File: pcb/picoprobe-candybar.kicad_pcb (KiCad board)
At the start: 2 copper layers, 27.9 x 97 mm, 39 parts, among them J0 SWD-UART_PicoprobeCandybar, J1 PinHeader_2x04, J2 PinSocket_1x03, J3 PinSocket_1x03, J4 PinSocket_1x03, J5 PinSocket_1x03, J6 PinSocket_1x03, J7 PinSocket_1x03, Q1 T2N7002AK, Q2 DMP31D1U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

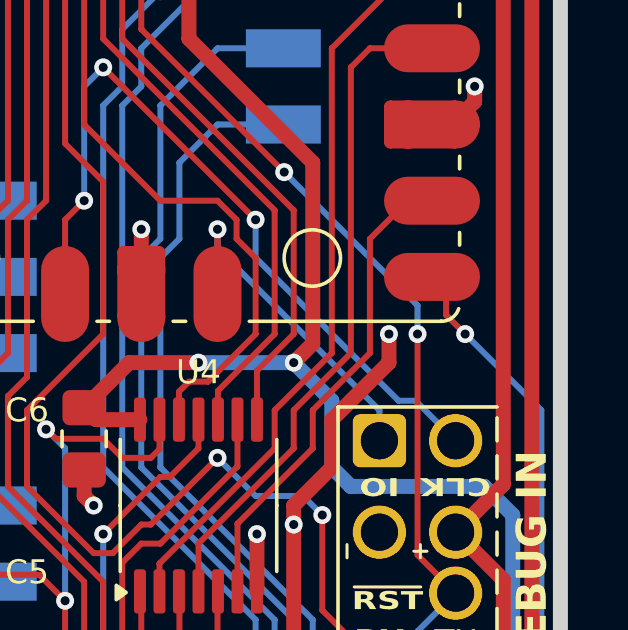
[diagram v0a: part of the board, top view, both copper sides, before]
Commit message: Change Q2 out for an available alternative
Original DMP31D1U was on backorder on Digi-Key.
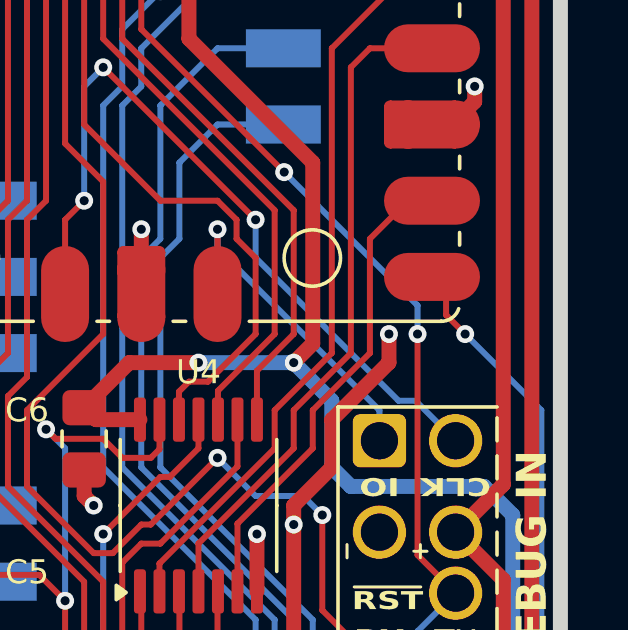
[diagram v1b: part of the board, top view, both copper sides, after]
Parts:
- Q2: value DMP31D1U -> GSFC02501
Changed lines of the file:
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@@
 		(fp_arc
 			(start 10.579676 25.189937)
-			(mid 10.357946 25.493957)
+			(mid 10.357958 25.493991)
 			(end 10 25.61)
 			(stroke
@@
 			)
 		)
-		(property "Value" "DMP31D1U"
+		(property "Value" "GSFC02501"
 			(at 0 2.4 90)
 			(layer "F.Fab")
@@
 			)
 		)
-		(property "Datasheet" "https://www.diodes.com/assets/Datasheets/DMP31D1U.pdf"
+		(property "Datasheet" "https://goodarksemi.com/docs/datasheets/mosfets/GSFC02501.pdf"
 			(at 0 0 -90)
 			(unlocked yes)
@@
 		(tags "capacitor handsolder")
 		(property "Reference" "C7"
-			(at -2.8575 -0.0635 360)
+			(at -2.8575 -0.0635 0)
 			(layer "F.SilkS")
 			(effects
@@
 		)
 		(property "Value" "1u"
-			(at 0 1.68 360)
+			(at 0 1.68 0)
 			(layer "F.Fab")
 			(effects
@@
 		)
 		(fp_text user "${REFERENCE}"
-			(at -0.635 0 360)
+			(at -0.635 0 0)
 			(layer "F.Fab")
 			(effects

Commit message: Update side output names to "PinHeader_1x03"
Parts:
- J2, J3, J4, J5, J6, J7: value PinSocket_1x03 -> PinHeader_1x03
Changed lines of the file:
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@@
 			)
 		)
-		(property "Value" "PinSocket_1x03"
+		(property "Value" "PinHeader_1x03"
 			(at 1.27 -5.08 180)
 			(unlocked yes)
@@
 			)
 		)
-		(property "Value" "PinSocket_1x03"
+		(property "Value" "PinHeader_1x03"
 			(at 1.27 -5.08 0)
 			(unlocked yes)
@@
 			)
 		)
-		(property "Value" "PinSocket_1x03"
+		(property "Value" "PinHeader_1x03"
 			(at 1.27 -5.08 180)
 			(unlocked yes)
@@
 			)
 		)
-		(property "Value" "PinSocket_1x03"
+		(property "Value" "PinHeader_1x03"
 			(at 1.27 -5.08 180)
 			(unlocked yes)
@@
 			)
 		)
-		(property "Value" "PinSocket_1x03"
+		(property "Value" "PinHeader_1x03"
 			(at 1.27 -5.08 180)
 			(unlocked yes)
@@
 			)
 		)
-		(property "Value" "PinSocket_1x03"
+		(property "Value" "PinHeader_1x03"
 			(at 1.27 -5.08 0)
 			(unlocked yes)

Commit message: Change Q1 out for a cheaper alternative
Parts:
- Q1: value T2N7002AK -> SSF2320Y
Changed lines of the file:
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@@
 			)
 		)
-		(property "Value" "T2N7002AK"
+		(property "Value" "SSF2320Y"
 			(at 0 2.4 90)
 			(layer "F.Fab")
@@
 			)
 		)
-		(property "Datasheet" "https://toshiba.semicon-storage.com/info/T2N7002AK_datasheet_en_20150401.pdf"
+		(property "Datasheet" "https://goodarksemi.com/docs/datasheets/mosfets/SSF2320Y.pdf"
 			(at 0 0 -90)
 			(unlocked yes)

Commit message: Update part names to fully resolved names
Tested via Digi-Key list upload:
<https://www.digikey.com/en/mylists/>
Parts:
- U3, U4: value SN74LV6T17 -> SN74LV6T17PWR
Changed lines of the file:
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@@
 			)
 		)
-		(property "Value" "SN74LV6T17"
+		(property "Value" "SN74LV6T17PWR"
 			(at 0 3.45 90)
 			(layer "F.Fab")
@@
 			)
 		)
-		(property "Manufacturer Part Number" "SN74LV6T17"
+		(property "Manufacturer Part Number" "SN74LV6T17PWR"
 			(at 0 0 -90)
 			(unlocked yes)
@@
 			)
 		)
-		(property "Value" "SN74LV6T17"
+		(property "Value" "SN74LV6T17PWR"
 			(at 0 3.45 90)
 			(layer "F.Fab")
@@
 			)
 		)
-		(property "Manufacturer Part Number" "SN74LV6T17"
+		(property "Manufacturer Part Number" "SN74LV6T17PWR"
 			(at 0 0 90)
 			(unlocked yes)
@@
 			)
 		)
-		(property "Manufacturer Part Number" "PMEG2010ER"
+		(property "Manufacturer Part Number" "PMEG2010ER,115"
 			(at 0 0 90)
 			(unlocked yes)
